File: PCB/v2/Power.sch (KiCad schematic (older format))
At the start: 19 parts, among them J4 Barrel_Jack_Switch, U3 TPS562200

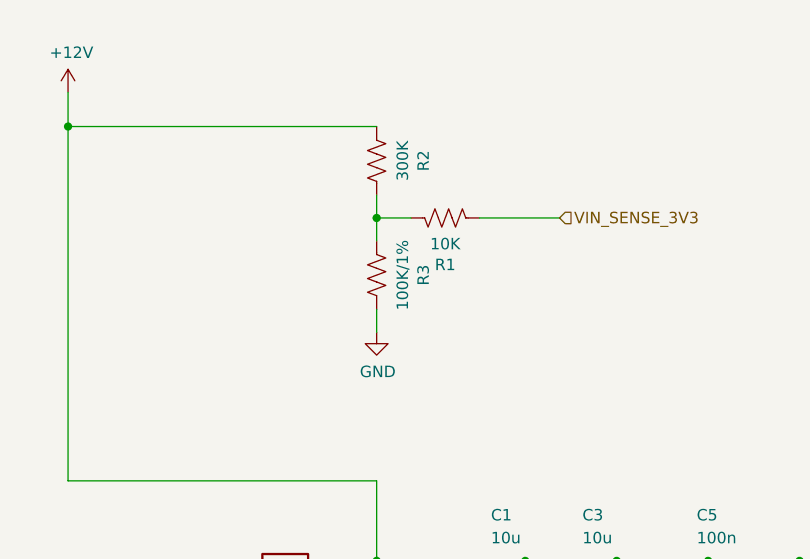
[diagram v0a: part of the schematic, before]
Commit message: Add 12V to ENN Loop
Added 12v detection to ENN loop, so EN on tmc would be high if 12v not present but 5v is.
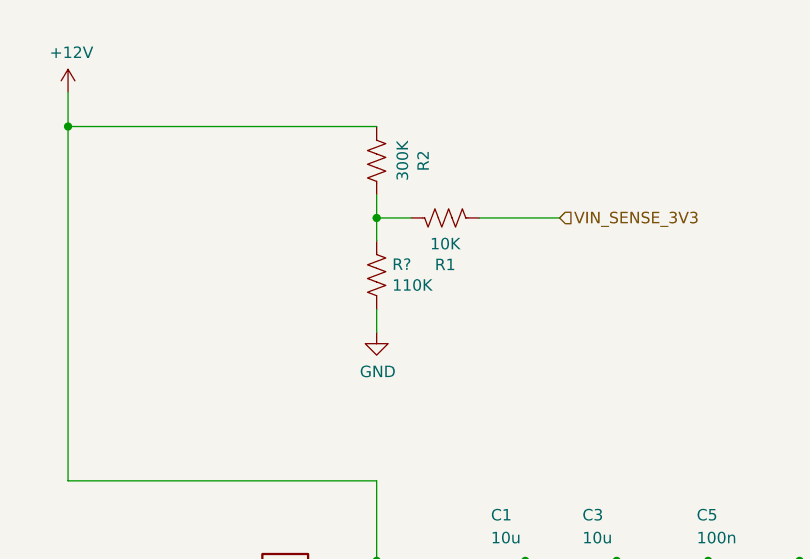
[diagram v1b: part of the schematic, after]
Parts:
- removed R3: 100K/1%, Resistor_SMD:R_0603_1608Metric, symbol MMTK-rescue:R_US-Device-MMTK-rescue-MMTK-rescue
- added R?: 110K, Resistor_SMD:R_0603_1608Metric, symbol MMTK-rescue:R_US-Device-MMTK-rescue-MMTK-rescue
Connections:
- net GND: now also R?.2
- net at R1.2, R2.1: now also R?.1
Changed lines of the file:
@@
-$EndComp
-$Comp
-L MMTK-rescue:R_US-Device-MMTK-rescue-MMTK-rescue R?
-U 1 1 5EE1FE67
-P 3500 3400
-AR Path="/5EBF47FB/5EE1FE67" Ref="R?"  Part="1"
-AR Path="/5EB8593E/5EE1FE67" Ref="R3"  Part="1"
-AR Path="/5F79E13B/5EE1FE67" Ref="R3"  Part="1"
-F 0 "R3" V 3295 3400 50  0000 C CNN
-F 1 "100K/1%" V 3386 3400 50  0000 C CNN
-F 2 "Resistor_SMD:R_0603_1608Metric" V 3540 3390 50  0001 C CNN
-F 3 "~" H 3500 3400 50  0001 C CNN
-	1    3500 3400
-	-1   0    0    1
 $EndComp
 $Comp
@@
 	-1   0    0    1
 $EndComp
+$Comp
+L MMTK-rescue:R_US-Device-MMTK-rescue-MMTK-rescue R?
+U 1 1 628D9011
+P 3500 3400
+F 0 "R?" H 3568 3446 50  0000 L CNN
+F 1 "110K" H 3568 3355 50  0000 L CNN
+F 2 "Resistor_SMD:R_0603_1608Metric" V 3540 3390 50  0001 C CNN
+F 3 "~" H 3500 3400 50  0001 C CNN
+	1    3500 3400
+	1    0    0    -1
+$EndComp
 $EndSCHEMATC
